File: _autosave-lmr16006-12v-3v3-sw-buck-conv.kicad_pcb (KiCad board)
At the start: 2 copper layers, 20 x 15 mm, 13 parts, among them U1 LMR16006XDDCR

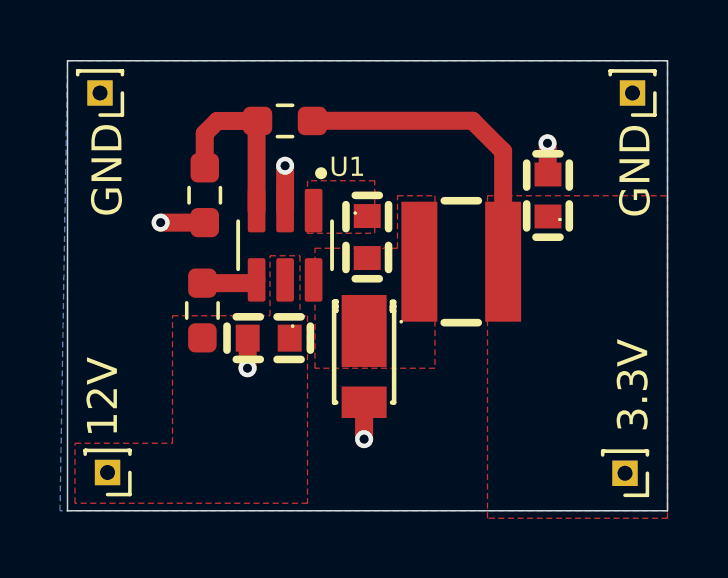
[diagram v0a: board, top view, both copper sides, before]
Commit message: Updated Layout with Additional GND Vias
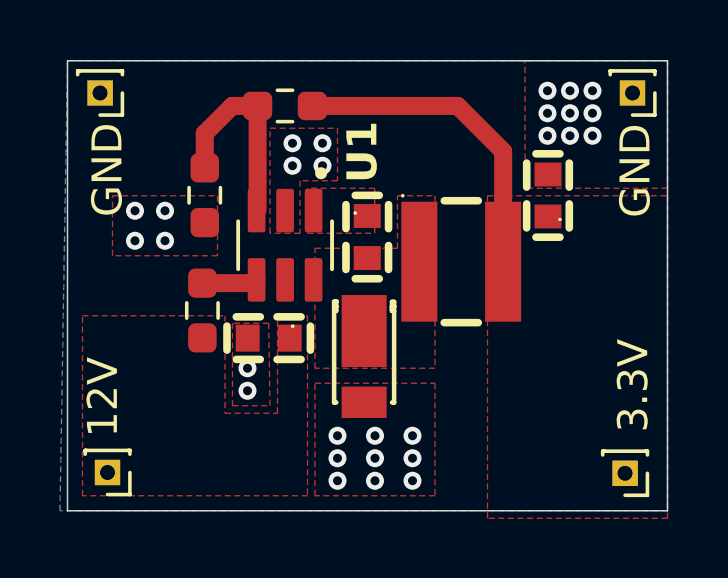
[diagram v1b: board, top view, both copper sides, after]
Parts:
- moved R2 0.50 mm to (87.2, 81.5)
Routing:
- net GND: track 6.24 -> 0.00 mm, vias 5 -> 28
- net Net-(U1-FB): track 5.94 -> 6.74 mm
- added copper zone on F.Cu, net GND
